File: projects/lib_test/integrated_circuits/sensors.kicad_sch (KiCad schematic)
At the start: 3 parts, among them U2001 ADXL345, U2002 ZXCT1010, U2003 LM335

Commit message: updated ic test project
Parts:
- renumbered U2002 to U2001, U2003 to U2002, U2001 to U2003
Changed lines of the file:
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@@
 	(title_block
 		(title "Integrated circuits")
-		(date "2026-01-06")
+		(date "2026-01-10")
 		(rev "1")
 		(comment 1 "-")
@@
 		(on_board yes)
 		(dnp no)
-		(property "Reference" "U2001"
+		(property "Reference" "U2003"
 			(at 40.64 24.13 0)
 			(effects
@@
 			(project ""
 				(path "/e63e39d7-6ac0-4ffd-8aa3-1841a4541b55/11447c1d-12bc-4b1f-be42-30d1ccb690a0"
-					(reference "U2001")
+					(reference "U2003")
 					(unit 1)
 				)
@@
 		(on_board yes)
 		(dnp no)
-		(property "Reference" "U2003"
+		(property "Reference" "U2002"
 			(at 116.84 29.21 0)
 			(effects
@@
 			(project ""
 				(path "/e63e39d7-6ac0-4ffd-8aa3-1841a4541b55/11447c1d-12bc-4b1f-be42-30d1ccb690a0"
-					(reference "U2003")
+					(reference "U2002")
 					(unit 1)
 				)
@@
 		(on_board yes)
 		(dnp no)
-		(property "Reference" "U2002"
+		(property "Reference" "U2001"
 			(at 92.71 30.48 0)
 			(effects
@@
 			(project ""
 				(path "/e63e39d7-6ac0-4ffd-8aa3-1841a4541b55/11447c1d-12bc-4b1f-be42-30d1ccb690a0"
-					(reference "U2002")
+					(reference "U2001")
 					(unit 1)
 				)

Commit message: updated test projects
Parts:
- renumbered U2001 to U1001, U2002 to U1002, U2003 to U1003
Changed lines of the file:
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@@
 		(on_board yes)
 		(dnp no)
-		(property "Reference" "U2003"
+		(property "Reference" "U1003"
 			(at 40.64 24.13 0)
 			(effects
@@
 			(project ""
 				(path "/e63e39d7-6ac0-4ffd-8aa3-1841a4541b55/11447c1d-12bc-4b1f-be42-30d1ccb690a0"
-					(reference "U2003")
+					(reference "U1003")
 					(unit 1)
 				)
@@
 		(on_board yes)
 		(dnp no)
-		(property "Reference" "U2002"
+		(property "Reference" "U1002"
 			(at 116.84 29.21 0)
 			(effects
@@
 			(project ""
 				(path "/e63e39d7-6ac0-4ffd-8aa3-1841a4541b55/11447c1d-12bc-4b1f-be42-30d1ccb690a0"
-					(reference "U2002")
+					(reference "U1002")
 					(unit 1)
 				)
@@
 		(on_board yes)
 		(dnp no)
-		(property "Reference" "U2001"
+		(property "Reference" "U1001"
 			(at 92.71 30.48 0)
 			(effects
@@
 			(project ""
 				(path "/e63e39d7-6ac0-4ffd-8aa3-1841a4541b55/11447c1d-12bc-4b1f-be42-30d1ccb690a0"
-					(reference "U2001")
+					(reference "U1001")
 					(unit 1)
 				)

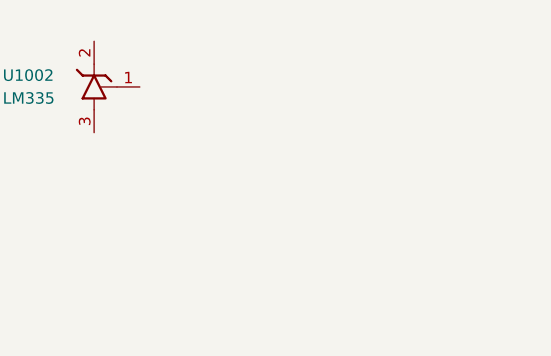
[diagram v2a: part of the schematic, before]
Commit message: add AT24QT1010 to test design
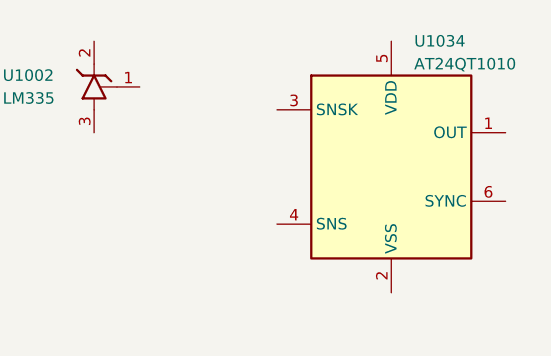
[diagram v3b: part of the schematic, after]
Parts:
- added U1034: AT24QT1010, lily_footprints:sot23-6_sc74, symbol lily_symbols:ic_touch_AT24QT1010_sot23-6
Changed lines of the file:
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@@
+	)
+	(symbol
+		(lib_id "lily_symbols:ic_touch_AT24QT1010_sot23-6")
+		(at 147.32 33.02 0)
+		(unit 1)
+		(exclude_from_sim no)
+		(in_bom yes)
+		(on_board yes)
+		(dnp no)
+		(property "Reference" "U1034"
+			(at 162.56 25.4 0)
+			(effects
+				(font
+					(size 1.27 1.27)
+				)
+				(justify left)
+			)
+		)
+		(property "Value" "AT24QT1010"
+			(at 162.56 27.94 0)
+			(effects
+				(font
+					(size 1.27 1.27)
+				)
+				(justify left)
+			)
+		)
+		(property "Footprint" "lily_footprints:sot23-6_sc74"
+			(at 160.02 68.58 0)
+			(effects
+				(font
+					(size 1.27 1.27)
+				)
+				(hide yes)
+			)
+		)
+		(property "Datasheet" "https://lilytronics.github.io/lily_kicad_lib/datasheets/microchip/AT42QT1010.pdf"
+			(at 160.02 81.28 0)
+			(effects
+				(font
+					(size 1.27 1.27)
+				)
+				(hide yes)
+			)
+		)
+		(property "Description" ""
+			(at 147.32 33.02 0)
+			(effects
+				(font
+					(size 1.27 1.27)
+				)
+				(hide yes)
+			)
+		)
+		(property "Revision" "1"
+			(at 160.02 63.5 0)
+			(effects
+				(font
+					(size 1.27 1.27)
+				)
+				(hide yes)
+			)
+		)
+		(property "Status" "Active"
+			(at 160.02 66.04 0)
+			(effects
+				(font
+					(size 1.27 1.27)
+				)
+				(hide yes)
+			)
+		)
+		(property "Manufacturer" "Microchip Tech"
+			(at 160.02 71.12 0)
+			(effects
+				(font
+					(size 1.27 1.27)
+				)
+				(hide yes)
+			)
+		)
+		(property "Manufacturer_ID" "AT42QT1010-TSH"
+			(at 160.02 73.66 0)
+			(effects
+				(font
+					(size 1.27 1.27)
+				)
+				(hide yes)
+			)
+		)
+		(property "Lily_ID" "NO_ID"
+			(at 160.02 76.2 0)
+			(effects
+				(font
+					(size 1.27 1.27)
+				)
+				(hide yes)
+			)
+		)
+		(property "JLCPCB_ID" "C74512"
+			(at 160.02 78.74 0)
+			(effects
+				(font
+					(size 1.27 1.27)
+				)
+				(hide yes)
+			)
+		)
+		(pin "5"
+		)
+		(pin "4"
+		)
+		(pin "3"
+		)
+		(pin "2"
+		)
+		(pin "1"
+		)
+		(pin "6"
+		)
+		(instances
+			(project ""
+				(path "/e63e39d7-6ac0-4ffd-8aa3-1841a4541b55/11447c1d-12bc-4b1f-be42-30d1ccb690a0"
+					(reference "U1034")
+					(unit 1)
+				)
+			)
+		)
 	)
 	(symbol
